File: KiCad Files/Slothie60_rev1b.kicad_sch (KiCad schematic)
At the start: 20 parts

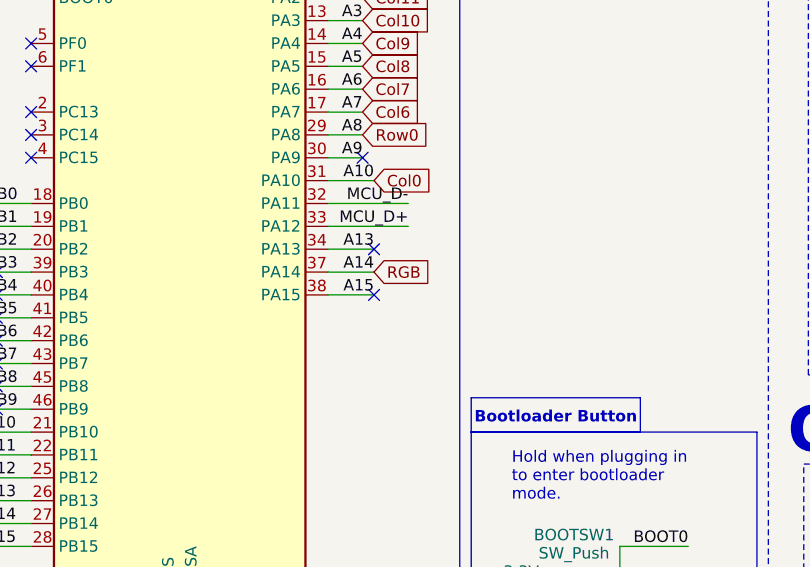
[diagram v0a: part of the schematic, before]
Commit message: Update to revision 1b
- Removed split space
- Updated to 16 5050-leds
- Changed to round routing
- Updated firmware
- Updated production and KiCad-folders to 9.0.1
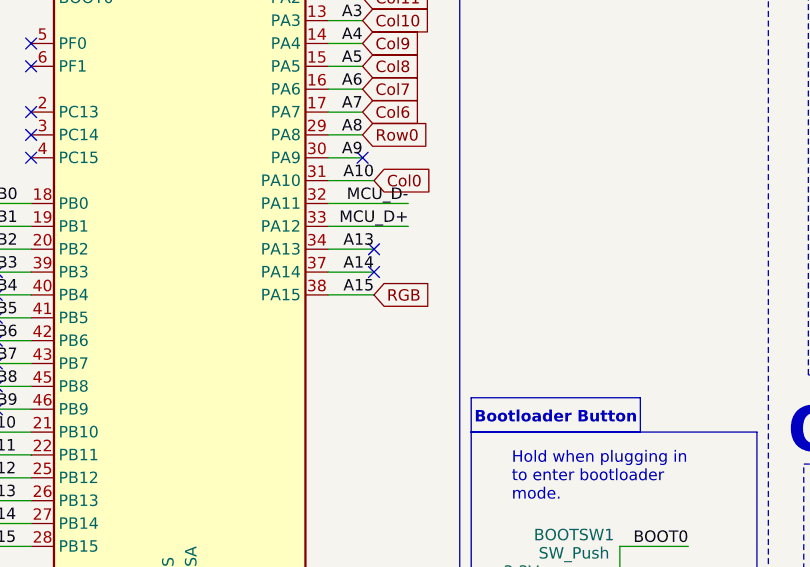
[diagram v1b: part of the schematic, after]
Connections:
- net A15 is gone; now on net RGB: MCU1.38 (PA15)
- net RGB: no longer MCU1.37 (PA14)
- new net A14: MCU1.37 (PA14)
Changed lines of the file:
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@@
 	)
 	(no_connect
-		(at 137.16 121.92)
-	)
-	(no_connect
 		(at 95.25 127)
 	)
@@
 	)
 	(no_connect
+		(at 137.16 119.38)
+	)
+	(no_connect
 		(at 99.06 101.6)
 	)
@@
 		)
 	)
+	(global_label "RGB"
+		(shape input)
+		(at 137.16 121.92 0)
+		(fields_autoplaced yes)
+		(effects
+			(font
+				(size 1.27 1.27)
+			)
+			(justify left)
+		)
+		(property "Intersheetrefs" "${INTERSHEET_REFS}"
+			(at 143.9552 121.92 0)
+			(effects
+				(font
+					(size 1.27 1.27)
+				)
+				(justify left)
+				(hide yes)
+			)
+		)
+	)
 	(global_label "Col4"
 		(shape input)
@@
 		)
 	)
-	(global_label "RGB"
-		(shape input)
-		(at 137.16 119.38 0)
-		(fields_autoplaced yes)
-		(effects
-			(font
-				(size 1.27 1.27)
-			)
-			(justify left)
-		)
-		(property "Intersheetrefs" "${INTERSHEET_REFS}"
-			(at 143.9552 119.38 0)
-			(effects
-				(font
-					(size 1.27 1.27)
-				)
-				(justify left)
-				(hide yes)
-			)
-		)
-	)
 	(global_label "Col7"
 		(shape input)
@@
 		)
 		(instances
-			(project "Slothie60_rev1a"
+			(project "Slothie60_rev1b"
 				(path "/9e336a8f-411c-4dde-8c95-c2c4ac1e5a1f"
 					(page "3")
@@
 		)
 		(instances
-			(project "Slothie60_rev1a"
+			(project "Slothie60_rev1b"
 				(path "/9e336a8f-411c-4dde-8c95-c2c4ac1e5a1f"
 					(page "2")
